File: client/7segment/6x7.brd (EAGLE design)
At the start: 78.4 x 61 mm, 26 parts, among them IC1 AT90S2313P, IC2 7805T

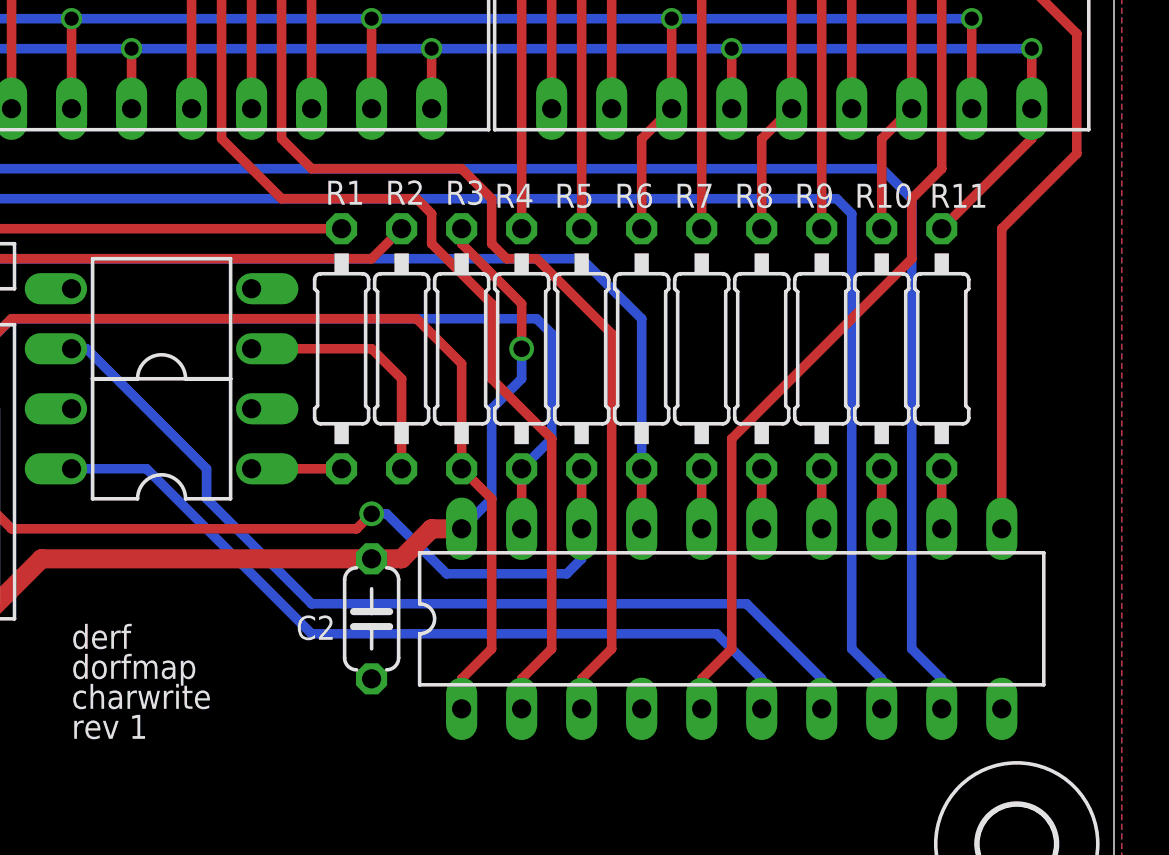
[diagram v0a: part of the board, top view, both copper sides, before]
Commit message: 7segment: Add external SDA/SCL pull-ups to allow higher clock rates
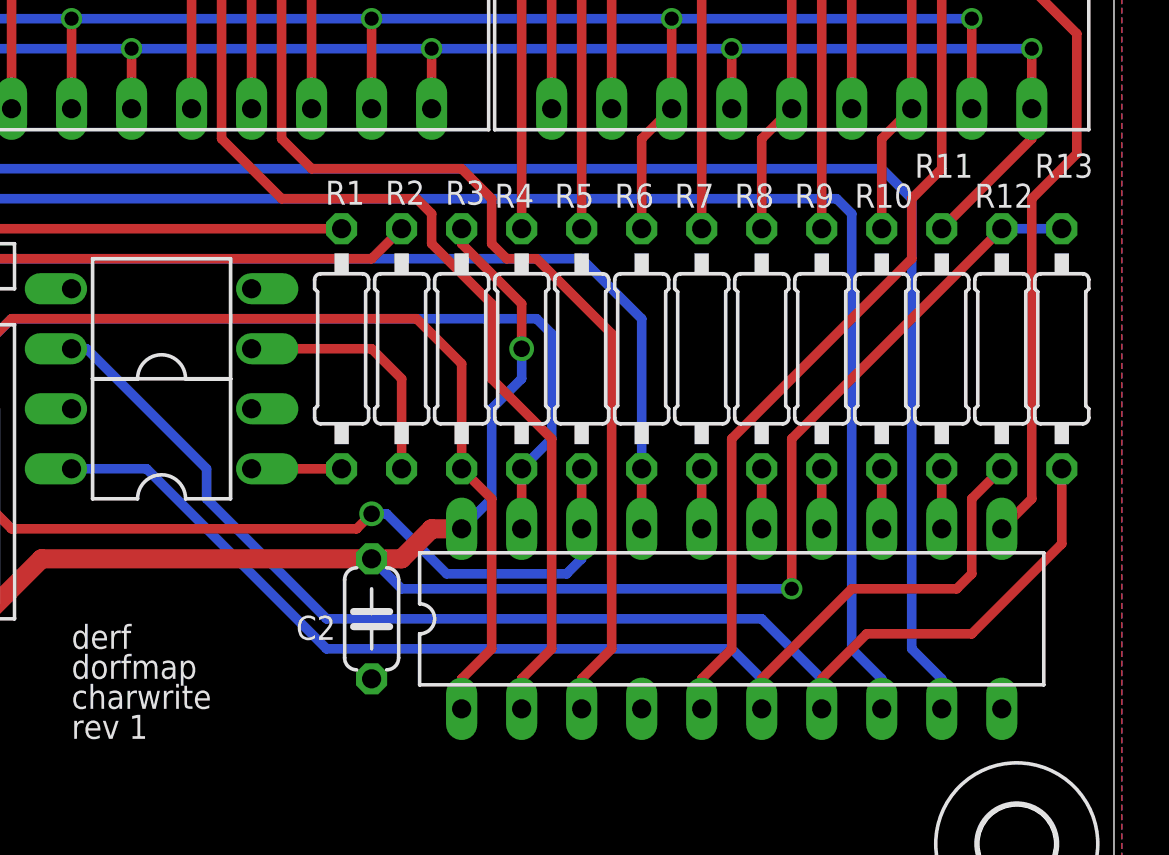
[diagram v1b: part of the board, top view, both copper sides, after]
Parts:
- added R12, R13: 3K3, rcl:0207/10
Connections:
- net 5V: now also R12.2, R13.2
- net AVRSCL: now also R12.1
- net AVRSDA: now also R13.1
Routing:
- net 5V: track 58.0 -> 97.8 mm, vias 1 -> 2
- net AVRSDA: track 39.6 -> 56.5 mm
- net AVRSCL: track 34.2 -> 51.1 mm
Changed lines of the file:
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@@
 <?xml version="1.0" encoding="utf-8"?>
 <!DOCTYPE eagle SYSTEM "eagle.dtd">
-<eagle version="6.6.0">
+<eagle version="7.5.0">
 <drawing>
 <settings>
@@
 <pass name="Default">
 <param name="RoutingGrid" value="50mil"/>
+<param name="AutoGrid" value="1"/>
+<param name="Efforts" value="0"/>
+<param name="TopRouterVariant" value="1"/>
 <param name="tpViaShape" value="round"/>
 <param name="PrefDir.1" value="|"/>
@@
 </element>
 <element name="R11" library="rcl" package="0207/10" value="470" x="71.12" y="25.4" smashed="yes" rot="R90">
-<attribute name="NAME" x="70.612" y="31.369" size="1.016" layer="25" ratio="10"/>
+<attribute name="NAME" x="69.977" y="32.639" size="1.016" layer="25" ratio="10"/>
 <attribute name="VALUE" x="71.755" y="23.1394" size="1.27" layer="27" ratio="10" rot="R90"/>
 </element>
@@
 <element name="H3" library="holes" package="3,2" value="MOUNT-HOLE3.2" x="4.445" y="56.515"/>
 <element name="H4" library="holes" package="3,2" value="MOUNT-HOLE3.2" x="74.295" y="56.515"/>
+<element name="R12" library="rcl" package="0207/10" value="3K3" x="73.66" y="25.4" smashed="yes" rot="R90">
+<attribute name="NAME" x="72.517" y="31.369" size="1.016" layer="25" ratio="10"/>
+<attribute name="VALUE" x="74.295" y="23.1394" size="1.27" layer="27" ratio="10" rot="R90"/>
+</element>
+<element name="R13" library="rcl" package="0207/10" value="3K3" x="76.2" y="25.4" smashed="yes" rot="R90">
+<attribute name="NAME" x="75.057" y="32.639" size="1.016" layer="25" ratio="10"/>
+<attribute name="VALUE" x="76.835" y="23.1394" size="1.27" layer="27" ratio="10" rot="R90"/>
+</element>
 </elements>
 <signals>
@@
 <contactref element="IC1" pad="6"/>
 <wire x1="34.29" y1="20.32" x2="37.465" y2="20.32" width="0.4064" layer="16"/>
-<wire x1="37.465" y1="20.32" x2="44.45" y2="13.335" width="0.4064" layer="16"/>
-<wire x1="44.45" y1="13.335" x2="61.595" y2="13.335" width="0.4064" layer="16"/>
-<wire x1="61.595" y1="13.335" x2="63.5" y2="11.43" width="0.4064" layer="16"/>
+<wire x1="37.465" y1="20.32" x2="45.085" y2="12.7" width="0.4064" layer="16"/>
+<wire x1="45.085" y1="12.7" x2="62.23" y2="12.7" width="0.4064" layer="16"/>
+<wire x1="62.23" y1="12.7" x2="63.5" y2="11.43" width="0.4064" layer="16"/>
 <wire x1="63.5" y1="11.43" x2="63.5" y2="10.16" width="0.4064" layer="16"/>
+<contactref element="R12" pad="1"/>
+<wire x1="73.66" y1="20.32" x2="72.39" y2="19.05" width="0.4064" layer="1"/>
+<wire x1="72.39" y1="19.05" x2="72.39" y2="15.875" width="0.4064" layer="1"/>
+<wire x1="72.39" y1="15.875" x2="71.755" y2="15.24" width="0.4064" layer="1"/>
+<wire x1="71.755" y1="15.24" x2="67.31" y2="15.24" width="0.4064" layer="1"/>
+<wire x1="67.31" y1="15.24" x2="63.5" y2="11.43" width="0.4064" layer="1"/>
+<wire x1="63.5" y1="11.43" x2="63.5" y2="10.16" width="0.4064" layer="1"/>
 </signal>
 <signal name="N$1">
@@
 <wire x1="52.07" y1="22.86" x2="52.07" y2="19.05" width="0.4064" layer="16"/>
 <wire x1="52.07" y1="19.05" x2="50.8" y2="17.78" width="0.4064" layer="16"/>
+<contactref element="R12" pad="2"/>
+<contactref element="R13" pad="2"/>
+<wire x1="76.2" y1="30.48" x2="73.66" y2="30.48" width="0.4064" layer="16"/>
+<wire x1="73.66" y1="30.48" x2="64.77" y2="21.59" width="0.4064" layer="1"/>
+<wire x1="64.77" y1="21.59" x2="64.77" y2="15.24" width="0.4064" layer="1"/>
+<via x="64.77" y="15.24" extent="1-16" drill="0.6"/>
+<wire x1="64.77" y1="15.24" x2="48.26" y2="15.24" width="0.4064" layer="16"/>
+<wire x1="48.26" y1="15.24" x2="46.99" y2="16.51" width="0.4064" layer="16"/>
 </signal>
 <signal name="AVRSDA">
@@
 <wire x1="34.925" y1="25.4" x2="40.005" y2="20.32" width="0.4064" layer="16"/>
 <wire x1="40.005" y1="20.32" x2="40.005" y2="19.05" width="0.4064" layer="16"/>
-<wire x1="40.005" y1="19.05" x2="44.45" y2="14.605" width="0.4064" layer="16"/>
-<wire x1="44.45" y1="14.605" x2="62.865" y2="14.605" width="0.4064" layer="16"/>
-<wire x1="62.865" y1="14.605" x2="66.04" y2="11.43" width="0.4064" layer="16"/>
+<wire x1="40.005" y1="19.05" x2="45.085" y2="13.97" width="0.4064" layer="16"/>
+<wire x1="45.085" y1="13.97" x2="63.5" y2="13.97" width="0.4064" layer="16"/>
+<wire x1="63.5" y1="13.97" x2="66.04" y2="11.43" width="0.4064" layer="16"/>
 <wire x1="66.04" y1="11.43" x2="66.04" y2="10.16" width="0.4064" layer="16"/>
+<contactref element="R13" pad="1"/>
+<wire x1="76.2" y1="20.32" x2="76.2" y2="17.145" width="0.4064" layer="1"/>
+<wire x1="76.2" y1="17.145" x2="72.39" y2="13.335" width="0.4064" layer="1"/>
+<wire x1="72.39" y1="13.335" x2="67.945" y2="13.335" width="0.4064" layer="1"/>
+<wire x1="67.945" y1="13.335" x2="66.04" y2="11.43" width="0.4064" layer="1"/>
+<wire x1="66.04" y1="11.43" x2="66.04" y2="10.16" width="0.4064" layer="1"/>
 </signal>
 <signal name="N$3">
@@
 <contactref element="IC1" pad="11"/>
 <contactref element="DIS3" pad="14"/>
-<wire x1="73.66" y1="17.78" x2="73.66" y2="30.48" width="0.4064" layer="1"/>
-<wire x1="73.66" y1="30.48" x2="76.835" y2="33.655" width="0.4064" layer="1"/>
 <wire x1="73.66" y1="41.91" x2="76.835" y2="38.735" width="0.4064" layer="1"/>
 <wire x1="76.835" y1="38.735" x2="76.835" y2="33.655" width="0.4064" layer="1"/>
@@
 <wire x1="65.405" y1="48.895" x2="64.77" y2="49.53" width="0.4064" layer="16"/>
 <wire x1="64.77" y1="49.53" x2="64.77" y2="50.8" width="0.4064" layer="16"/>
+<wire x1="76.835" y1="33.655" x2="74.93" y2="31.75" width="0.4064" layer="1"/>
+<wire x1="74.93" y1="31.75" x2="74.93" y2="19.05" width="0.4064" layer="1"/>
+<wire x1="74.93" y1="19.05" x2="73.66" y2="17.78" width="0.4064" layer="1"/>
 </signal>
 <signal name="D5">
